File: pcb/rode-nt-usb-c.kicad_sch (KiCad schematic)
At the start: 7 parts, among them J1 USB_C_Receptacle_USB2.0_16P, J2 Conn_01x05_Pin

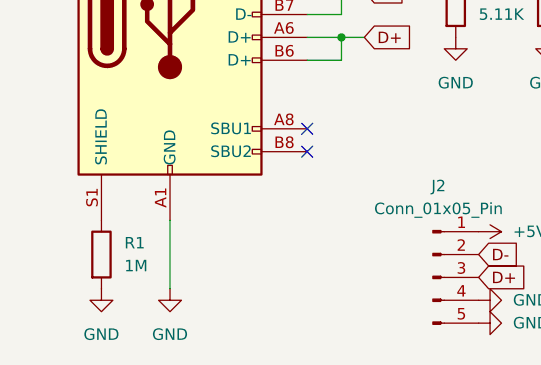
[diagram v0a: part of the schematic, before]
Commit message: Remove R1, update overall design
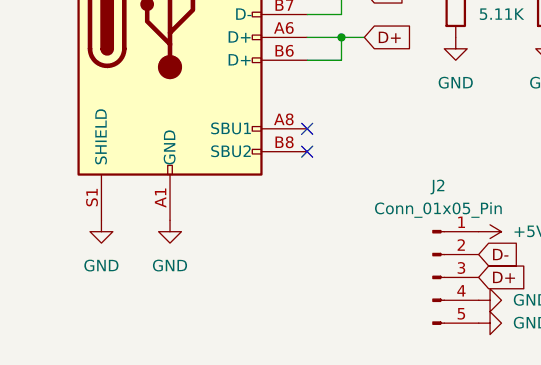
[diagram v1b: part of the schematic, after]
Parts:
- removed R1: 1M, Resistor_SMD:R_1206_3216Metric_Pad1.30x1.75mm_HandSolder, symbol Device:R
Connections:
- net GND: now also J1.S1 (SHIELD)
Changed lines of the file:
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@@
 	(wire
 		(pts
-			(xy 86.36 116.84) (xy 86.36 109.22)
+			(xy 101.6 86.36) (xy 105.41 86.36)
 		)
 		(stroke
@@
 	(wire
 		(pts
-			(xy 101.6 86.36) (xy 105.41 86.36)
+			(xy 101.6 76.2) (xy 128.27 76.2)
 		)
 		(stroke
@@
 	(wire
 		(pts
-			(xy 101.6 76.2) (xy 128.27 76.2)
+			(xy 125.73 71.12) (xy 106.68 71.12)
 		)
 		(stroke
@@
 	(wire
 		(pts
-			(xy 125.73 71.12) (xy 106.68 71.12)
+			(xy 118.11 78.74) (xy 118.11 81.28)
 		)
 		(stroke
@@
 	(wire
 		(pts
-			(xy 118.11 78.74) (xy 118.11 81.28)
+			(xy 125.73 63.5) (xy 120.65 63.5)
 		)
 		(stroke
@@
 	(wire
 		(pts
-			(xy 125.73 63.5) (xy 120.65 63.5)
+			(xy 101.6 78.74) (xy 118.11 78.74)
 		)
 		(stroke
@@
 	(wire
 		(pts
-			(xy 101.6 78.74) (xy 118.11 78.74)
+			(xy 105.41 91.44) (xy 105.41 88.9)
 		)
 		(stroke
@@
 		)
 	)
-	(wire
-		(pts
-			(xy 105.41 91.44) (xy 105.41 88.9)
-		)
-		(stroke
-			(width 0)
-			(type default)
-		)
-	)
 	(global_label "D+"
 		(shape input)
@@
 	(symbol
 		(lib_id "power:GND")
-		(at 78.74 116.84 0)
+		(at 78.74 109.22 0)
 		(unit 1)
 		(exclude_from_sim no)
@@
 		(fields_autoplaced yes)
 		(property "Reference" "#PWR03"
-			(at 78.74 123.19 0)
+			(at 78.74 115.57 0)
 			(effects
 				(font
@@
 		)
 		(property "Value" "GND"
-			(at 78.74 121.92 0)
+			(at 78.74 114.3 0)
 			(effects
 				(font
@@
 		)
 		(property "Footprint" ""
-			(at 78.74 116.84 0)
+			(at 78.74 109.22 0)
 			(effects
 				(font
@@
 		)
 		(property "Datasheet" ""
-			(at 78.74 116.84 0)
+			(at 78.74 109.22 0)
 			(effects
 				(font
@@
 		)
 		(property "Description" "Power symbol creates a global label with name \"GND\" , ground"
-			(at 78.74 116.84 0)
+			(at 78.74 109.22 0)
 			(effects
 				(font
@@
 	)
 	(symbol
-		(lib_id "Device:R")
-		(at 78.74 113.03 0)
-		(unit 1)
-		(exclude_from_sim no)
-		(in_bom yes)
-		(on_board yes)
-		(dnp no)
-		(fields_autoplaced yes)
-		(property "Reference" "R1"
-			(at 81.28 111.7599 0)
-			(effects
-				(font
-					(size 1.27 1.27)
-				)
-				(justify left)
-			)
-		)
-		(property "Value" "1M"
-			(at 81.28 114.2999 0)
-			(effects
-				(font
-					(size 1.27 1.27)
-				)
-				(justify left)
-			)
-		)
-		(property "Footprint" "Resistor_SMD:R_1206_3216Metric_Pad1.30x1.75mm_HandSolder"
-			(at 76.962 113.03 90)
-			(effects
-				(font
-					(size 1.27 1.27)
-				)
-				(hide yes)
-			)
-		)
-		(property "Datasheet" "~"
-			(at 78.74 113.03 0)
-			(effects
-				(font
-					(size 1.27 1.27)
-				)
-				(hide yes)
-			)
-		)
-		(property "Description" "Resistor"
-			(at 78.74 113.03 0)
-			(effects
-				(font
-					(size 1.27 1.27)
-				)
-				(hide yes)
-			)
-		)
-		(pin "2"
-		)
-		(pin "1"
-		)
-		(instances
-			(project "rode-nt-usb-c"
-				(path "/65483df2-e61e-4f34-9202-fac169fa34d7"
-					(reference "R1")
-					(unit 1)
-				)
-			)
-		)
-	)
-	(symbol
 		(lib_id "power:+5V")
 		(at 125.73 71.12 270)
@@
 	(symbol
 		(lib_id "power:GND")
-		(at 86.36 116.84 0)
+		(at 86.36 109.22 0)
 		(unit 1)
 		(exclude_from_sim no)
@@
 		(fields_autoplaced yes)
 		(property "Reference" "#PWR01"
-			(at 86.36 123.19 0)
+			(at 86.36 115.57 0)
 			(effects
 				(font
@@
 		)
 		(property "Value" "GND"
-			(at 86.36 121.92 0)
+			(at 86.36 114.3 0)
 			(effects
 				(font
@@
 		)
 		(property "Footprint" ""
-			(at 86.36 116.84 0)
+			(at 86.36 109.22 0)
 			(effects
 				(font
@@
 		)
 		(property "Datasheet" ""
-			(at 86.36 116.84 0)
+			(at 86.36 109.22 0)
 			(effects
 				(font
@@
 		)
 		(property "Description" "Power symbol creates a global label with name \"GND\" , ground"
-			(at 86.36 116.84 0)
-			(effects
-				(font
+			(at 86.36 109.22 0)
+			(effects
+				(font

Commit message: Change design, multiple adjustments
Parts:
- renumbered R2 to R1, R3 to R2, R4 to R3
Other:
- title: (none) -> RODE NT-USB-C
- moved on the sheet: D1, J1, J2, R1, R2, R3
